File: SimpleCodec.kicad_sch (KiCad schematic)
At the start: 7 parts, among them J1 RPI_ADC, J2 RP_GPIO

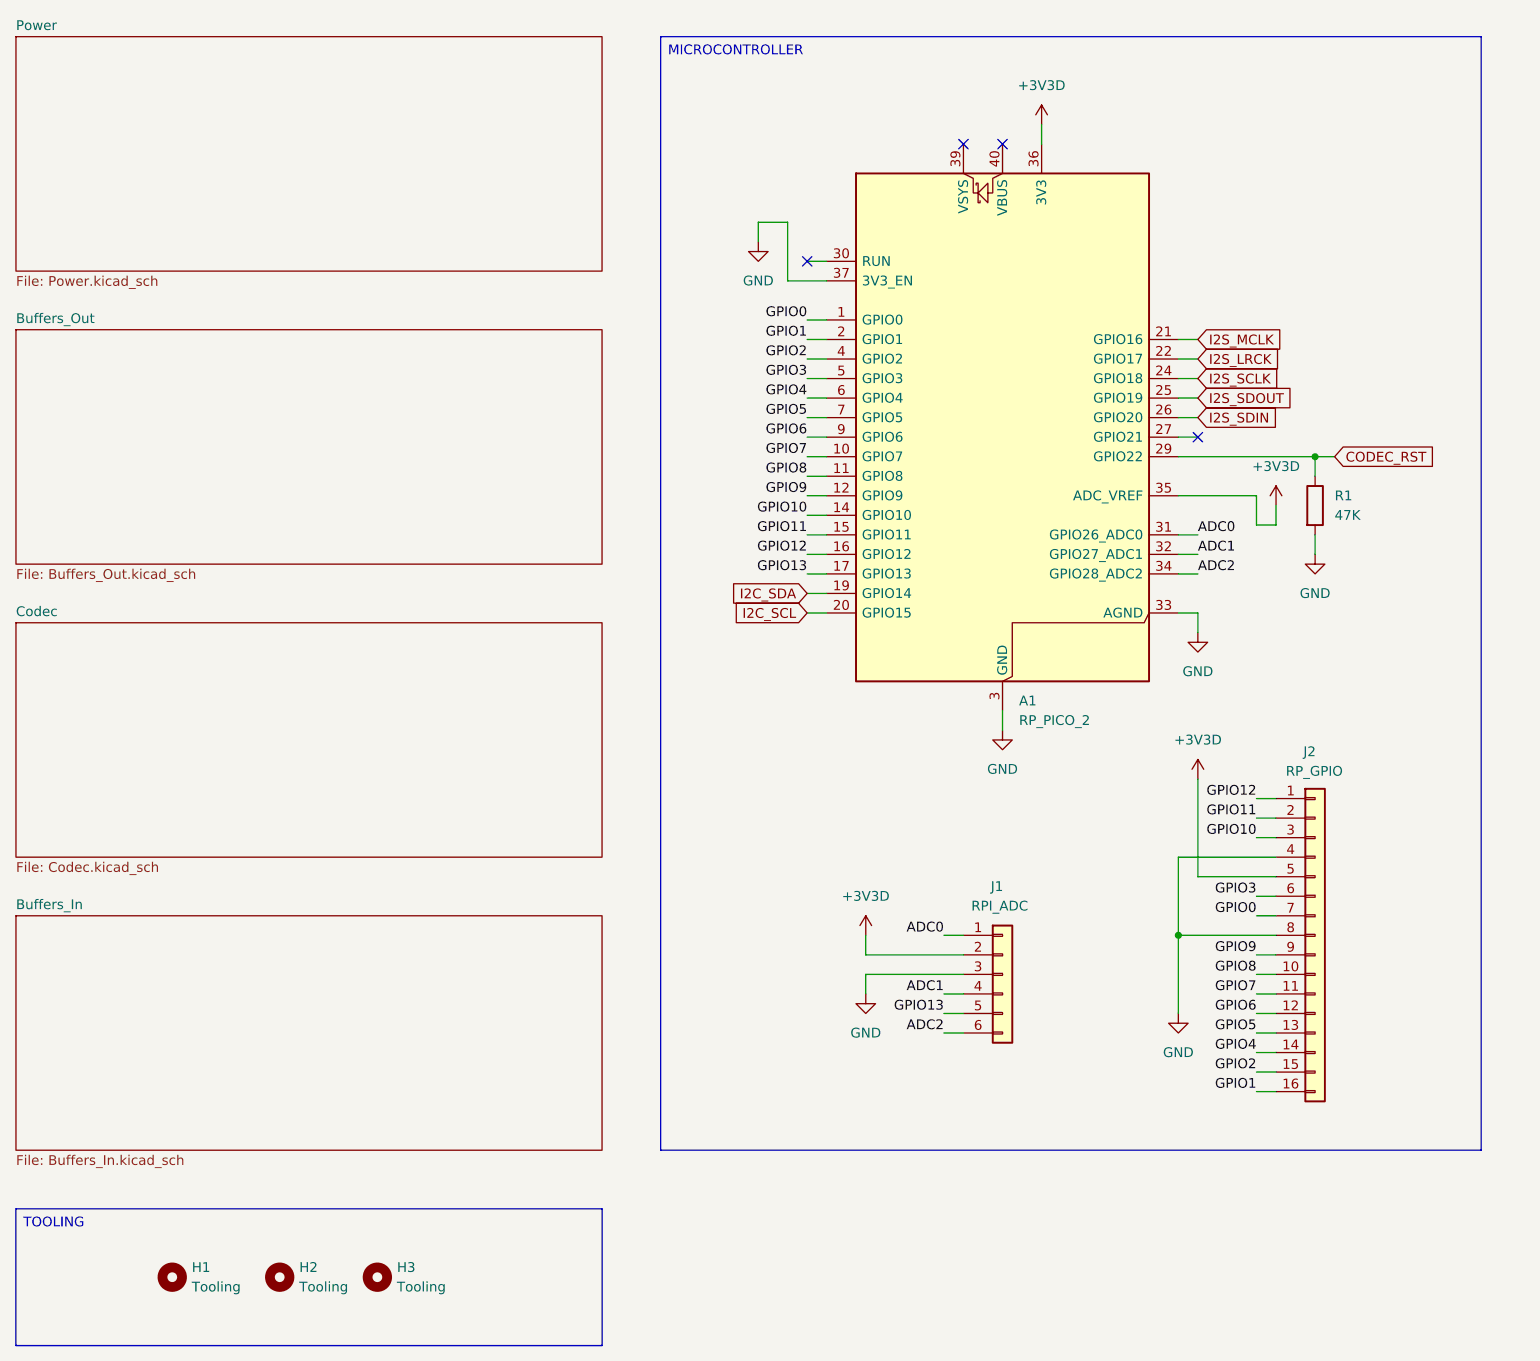
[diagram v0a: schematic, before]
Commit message: Initial mounting holes
Added some minimal mounting holes.
Need to review the positioning.
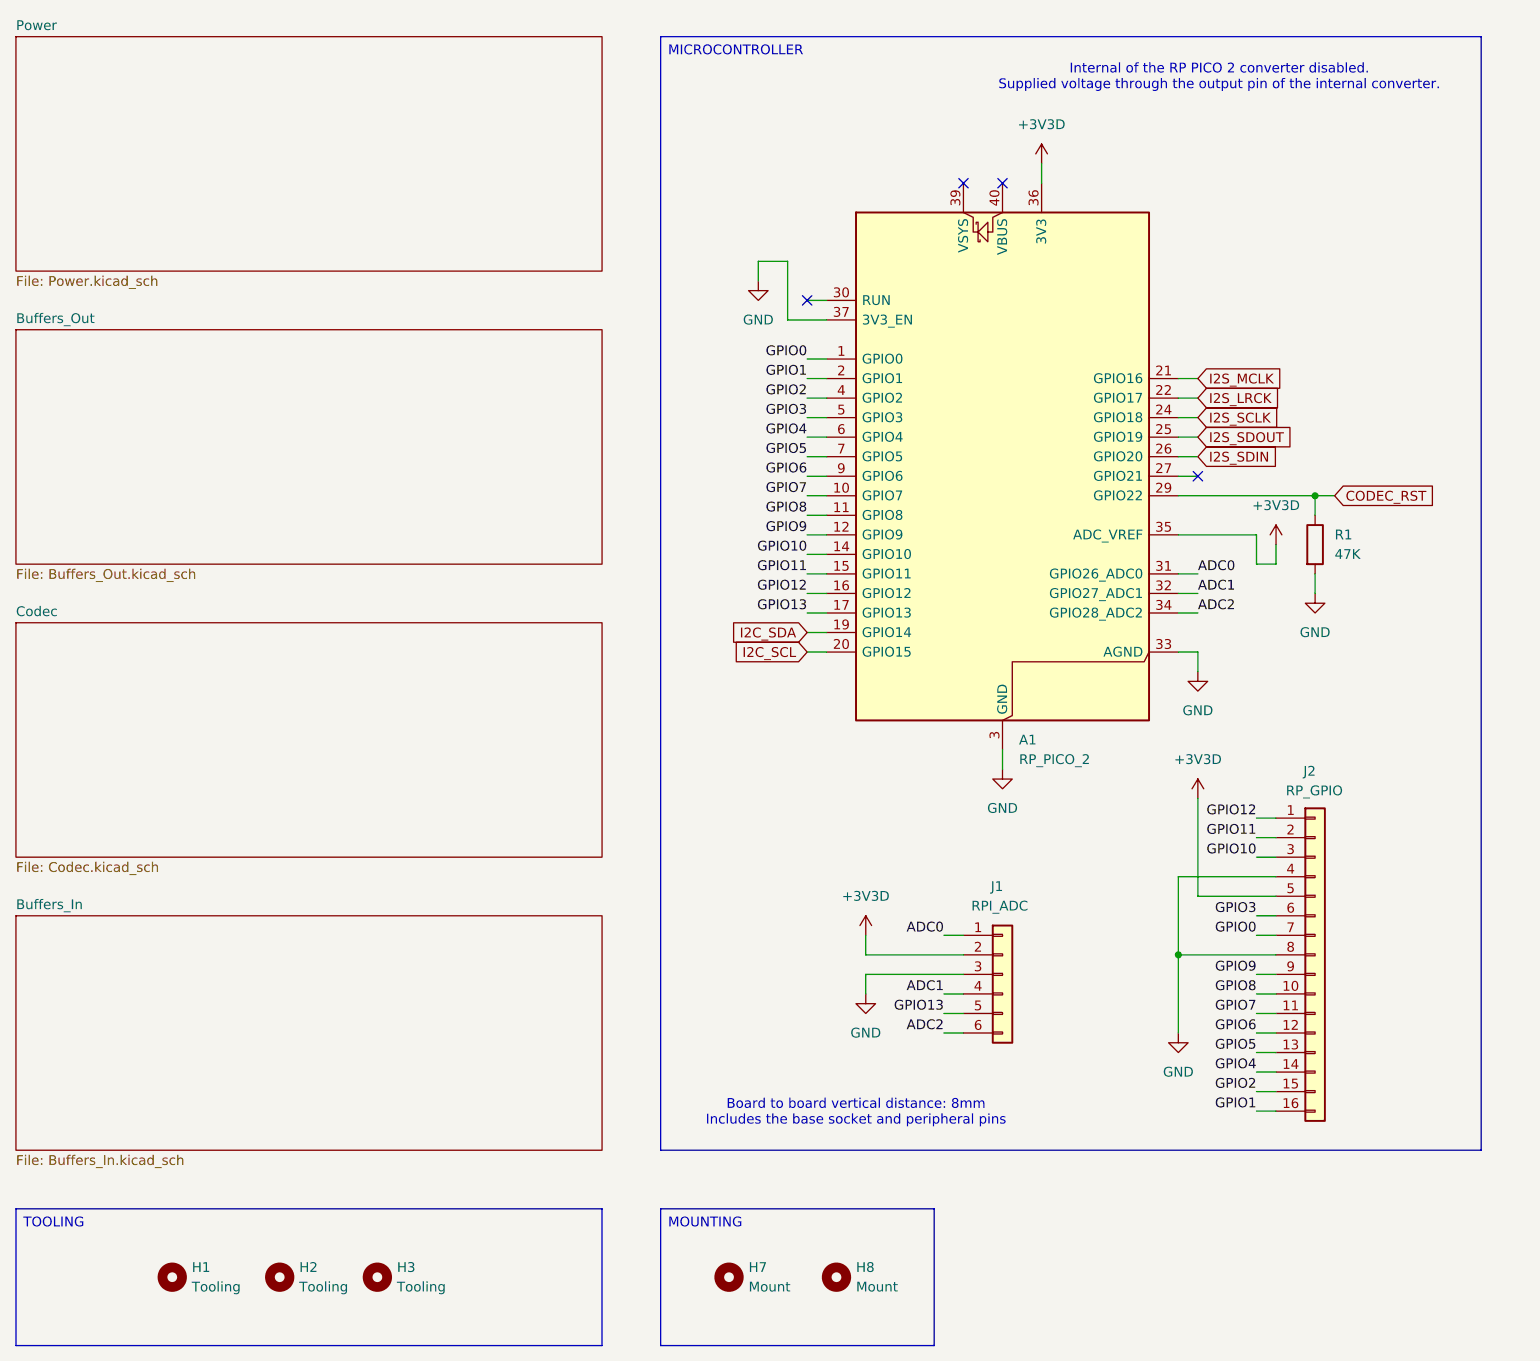
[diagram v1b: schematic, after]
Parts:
- added H7, H8: Mount, MountingHole:MountingHole_2.2mm_M2, symbol Mechanical:MountingHole
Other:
- note added: "Board to board vertical distance: 8mm Includes the base socket and peripheral pins"
- note added: "Internal of the RP PICO 2 converter disabled. Supplied voltage through the output pin of the internal converter."
- moved on the sheet: A1, J2, R1

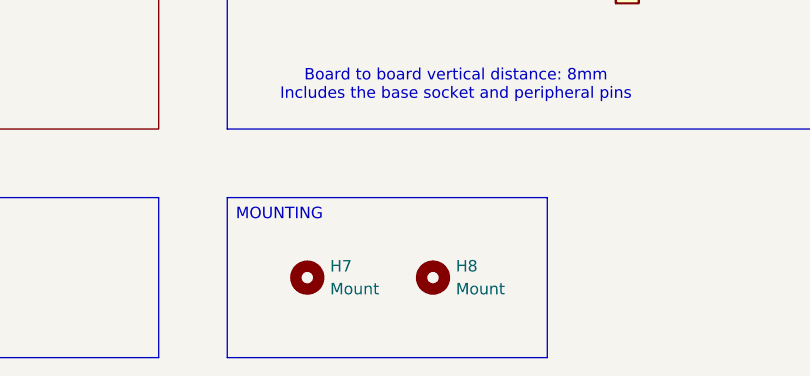
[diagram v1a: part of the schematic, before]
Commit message: Silkscreen design
Updated the silkscreen for the PCB.
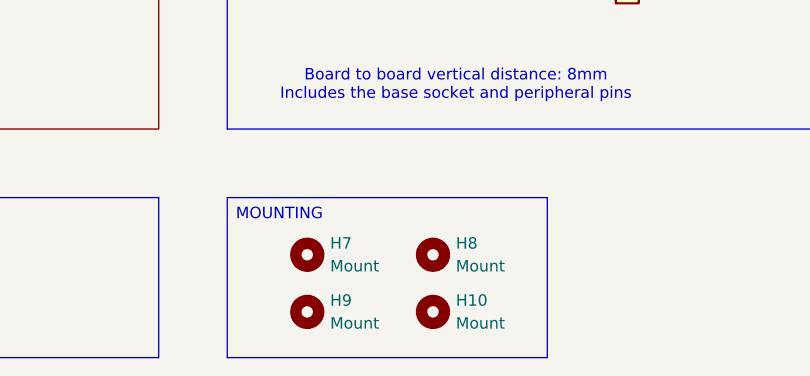
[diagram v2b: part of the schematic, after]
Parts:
- added H10, H9: Mount, MountingHole:MountingHole_2.2mm_M2, symbol Mechanical:MountingHole
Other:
- moved on the sheet: H7, H8
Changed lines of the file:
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@@
 	(symbol
 		(lib_id "Mechanical:MountingHole")
-		(at 158.75 179.07 0)
+		(at 158.75 176.53 0)
 		(unit 1)
 		(body_style 1)
@@
 		(fields_autoplaced yes)
 		(property "Reference" "H8"
+			(at 161.29 175.2599 0)
+			(show_name no)
+			(do_not_autoplace no)
+			(effects
+				(font
+					(size 1.27 1.27)
+				)
+				(justify left)
+			)
+		)
+		(property "Value" "Mount"
 			(at 161.29 177.7999 0)
 			(show_name no)
@@
 			)
 		)
-		(property "Value" "Mount"
-			(at 161.29 180.3399 0)
-			(show_name no)
-			(do_not_autoplace no)
-			(effects
-				(font
-					(size 1.27 1.27)
-				)
-				(justify left)
-			)
-		)
 		(property "Footprint" "MountingHole:MountingHole_2.2mm_M2"
-			(at 158.75 179.07 0)
-			(hide yes)
-			(show_name no)
-			(do_not_autoplace no)
-			(effects
-				(font
-					(size 1.27 1.27)
-				)
-			)
-		)
-		(property "Datasheet" ""
-			(at 158.75 179.07 0)
+			(at 158.75 176.53 0)
+			(hide yes)
+			(show_name no)
+			(do_not_autoplace no)
+			(effects
+				(font
+					(size 1.27 1.27)
+				)
+			)
+		)
+		(property "Datasheet" ""
+			(at 158.75 176.53 0)
 			(hide yes)
 			(show_name no)
@@
 		)
 		(property "Description" "Mounting Hole without connection"
-			(at 158.75 179.07 0)
+			(at 158.75 176.53 0)
 			(hide yes)
 			(show_name no)
@@
 	)
 	(symbol
+		(lib_id "Mechanical:MountingHole")
+		(at 158.75 182.88 0)
+		(unit 1)
+		(body_style 1)
+		(exclude_from_sim no)
+		(in_bom no)
+		(on_board yes)
+		(in_pos_files yes)
+		(dnp no)
+		(fields_autoplaced yes)
+		(property "Reference" "H10"
+			(at 161.29 181.6099 0)
+			(show_name no)
+			(do_not_autoplace no)
+			(effects
+				(font
+					(size 1.27 1.27)
+				)
+				(justify left)
+			)
+		)
+		(property "Value" "Mount"
+			(at 161.29 184.1499 0)
+			(show_name no)
+			(do_not_autoplace no)
+			(effects
+				(font
+					(size 1.27 1.27)
+				)
+				(justify left)
+			)
+		)
+		(property "Footprint" "MountingHole:MountingHole_2.2mm_M2"
+			(at 158.75 182.88 0)
+			(hide yes)
+			(show_name no)
+			(do_not_autoplace no)
+			(effects
+				(font
+					(size 1.27 1.27)
+				)
+			)
+		)
+		(property "Datasheet" ""
+			(at 158.75 182.88 0)
+			(hide yes)
+			(show_name no)
+			(do_not_autoplace no)
+			(effects
+				(font
+					(size 1.27 1.27)
+				)
+			)
+		)
+		(property "Description" "Mounting Hole without connection"
+			(at 158.75 182.88 0)
+			(hide yes)
+			(show_name no)
+			(do_not_autoplace no)
+			(effects
+				(font
+					(size 1.27 1.27)
+				)
+			)
+		)
+		(instances
+			(project "SimpleCodec"
+				(path "/4cbf131b-42e8-4a05-beea-68c6d66cdb1a"
+					(reference "H10")
+					(unit 1)
+				)
+			)
+		)
+	)
+	(symbol
+		(lib_id "Mechanical:MountingHole")
+		(at 144.78 182.88 0)
+		(unit 1)
+		(body_style 1)
+		(exclude_from_sim no)
+		(in_bom no)
+		(on_board yes)
+		(in_pos_files yes)
+		(dnp no)
+		(fields_autoplaced yes)
+		(property "Reference" "H9"
+			(at 147.32 181.6099 0)
+			(show_name no)
+			(do_not_autoplace no)
+			(effects
+				(font
+					(size 1.27 1.27)
+				)
+				(justify left)
+			)
+		)
+		(property "Value" "Mount"
+			(at 147.32 184.1499 0)
+			(show_name no)
+			(do_not_autoplace no)
+			(effects
+				(font
+					(size 1.27 1.27)
+				)
+				(justify left)
+			)
+		)
+		(property "Footprint" "MountingHole:MountingHole_2.2mm_M2"
+			(at 144.78 182.88 0)
+			(hide yes)
+			(show_name no)
+			(do_not_autoplace no)
+			(effects
+				(font
+					(size 1.27 1.27)
+				)
+			)
+		)
+		(property "Datasheet" ""
+			(at 144.78 182.88 0)
+			(hide yes)
+			(show_name no)
+			(do_not_autoplace no)
+			(effects
+				(font
+					(size 1.27 1.27)
+				)
+			)
+		)
+		(property "Description" "Mounting Hole without connection"
+			(at 144.78 182.88 0)
+			(hide yes)
+			(show_name no)
+			(do_not_autoplace no)
+			(effects
+				(font
+					(size 1.27 1.27)
+				)
+			)
+		)
+		(instances
+			(project "SimpleCodec"
+				(path "/4cbf131b-42e8-4a05-beea-68c6d66cdb1a"
+					(reference "H9")
+					(unit 1)
+				)
+			)
+		)
+	)
+	(symbol
 		(lib_id "power:+3.3V")
 		(at 215.9 83.82 0)
@@
 	(symbol
 		(lib_id "Mechanical:MountingHole")
-		(at 144.78 179.07 0)
+		(at 144.78 176.53 0)
 		(unit 1)
 		(body_style 1)
@@
 		(fields_autoplaced yes)
 		(property "Reference" "H7"
+			(at 147.32 175.2599 0)
+			(show_name no)
+			(do_not_autoplace no)
+			(effects
+				(font
+					(size 1.27 1.27)
+				)
+				(justify left)
+			)
+		)
+		(property "Value" "Mount"
 			(at 147.32 177.7999 0)
 			(show_name no)
@@
 			)
 		)
-		(property "Value" "Mount"
-			(at 147.32 180.3399 0)
-			(show_name no)
-			(do_not_autoplace no)
-			(effects
-				(font
-					(size 1.27 1.27)
-				)
-				(justify left)
-			)
-		)
 		(property "Footprint" "MountingHole:MountingHole_2.2mm_M2"
-			(at 144.78 179.07 0)
-			(hide yes)
-			(show_name no)
-			(do_not_autoplace no)
-			(effects
-				(font
-					(size 1.27 1.27)
-				)
-			)
-		)
-		(property "Datasheet" ""
-			(at 144.78 179.07 0)
+			(at 144.78 176.53 0)
+			(hide yes)
+			(show_name no)
+			(do_not_autoplace no)
+			(effects
+				(font
+					(size 1.27 1.27)
+				)
+			)
+		)
+		(property "Datasheet" ""
+			(at 144.78 176.53 0)
 			(hide yes)
 			(show_name no)
@@
 		)
 		(property "Description" "Mounting Hole without connection"
-			(at 144.78 179.07 0)
-			(hide yes)
-			(show_name no)
+			(at 144.78 176.53 0)
+			(hide yes)
+			(show_name no)
